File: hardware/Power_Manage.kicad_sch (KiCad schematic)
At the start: 59 parts, among them U10 TPS62088, U4 TPS62088, U6 MAX38904C, U7 MAX38904C, U8 TPS62088, U9 TPS62088

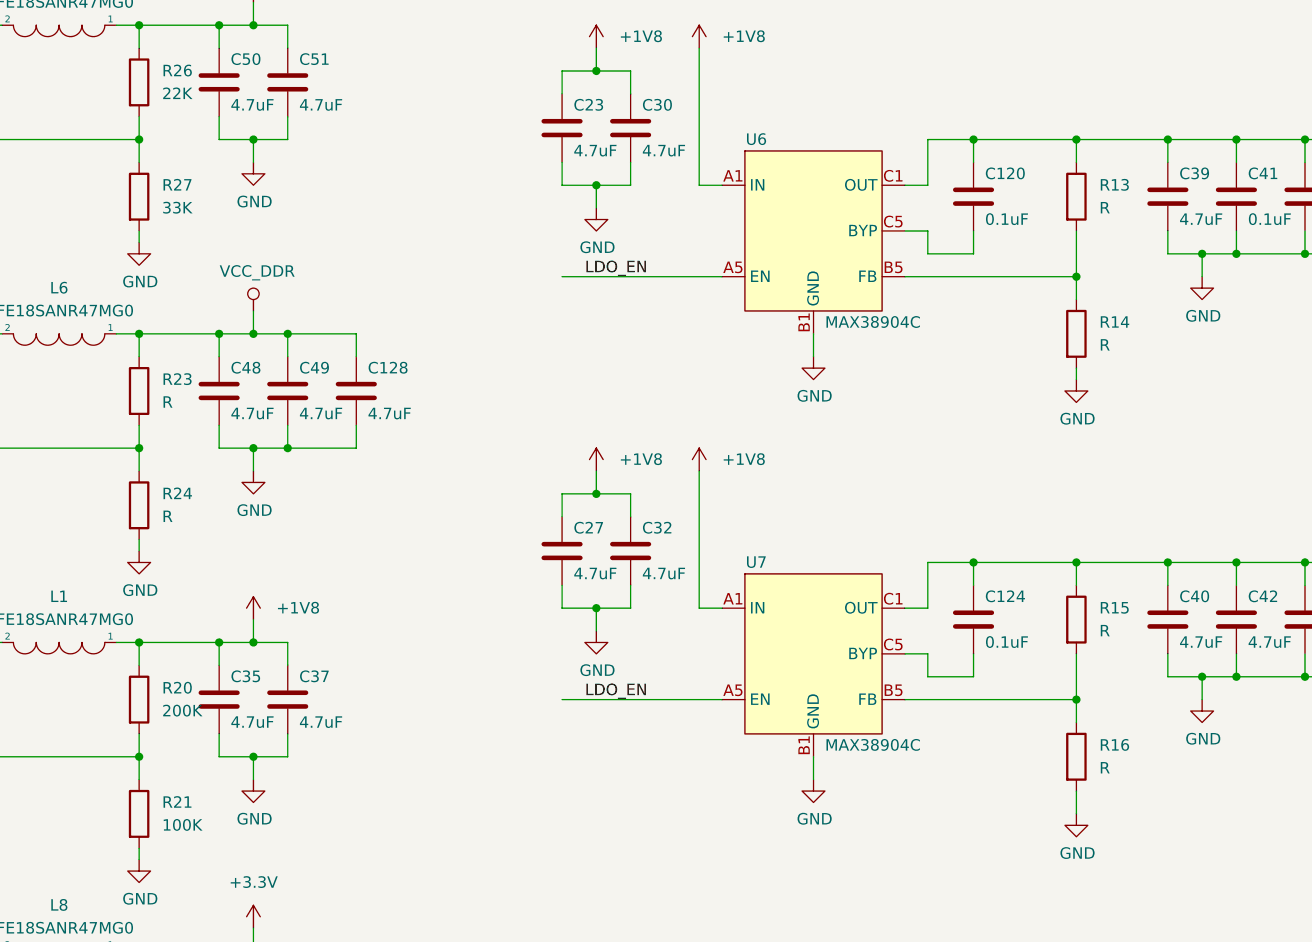
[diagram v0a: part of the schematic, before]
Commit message: add sdio level shift ciruit
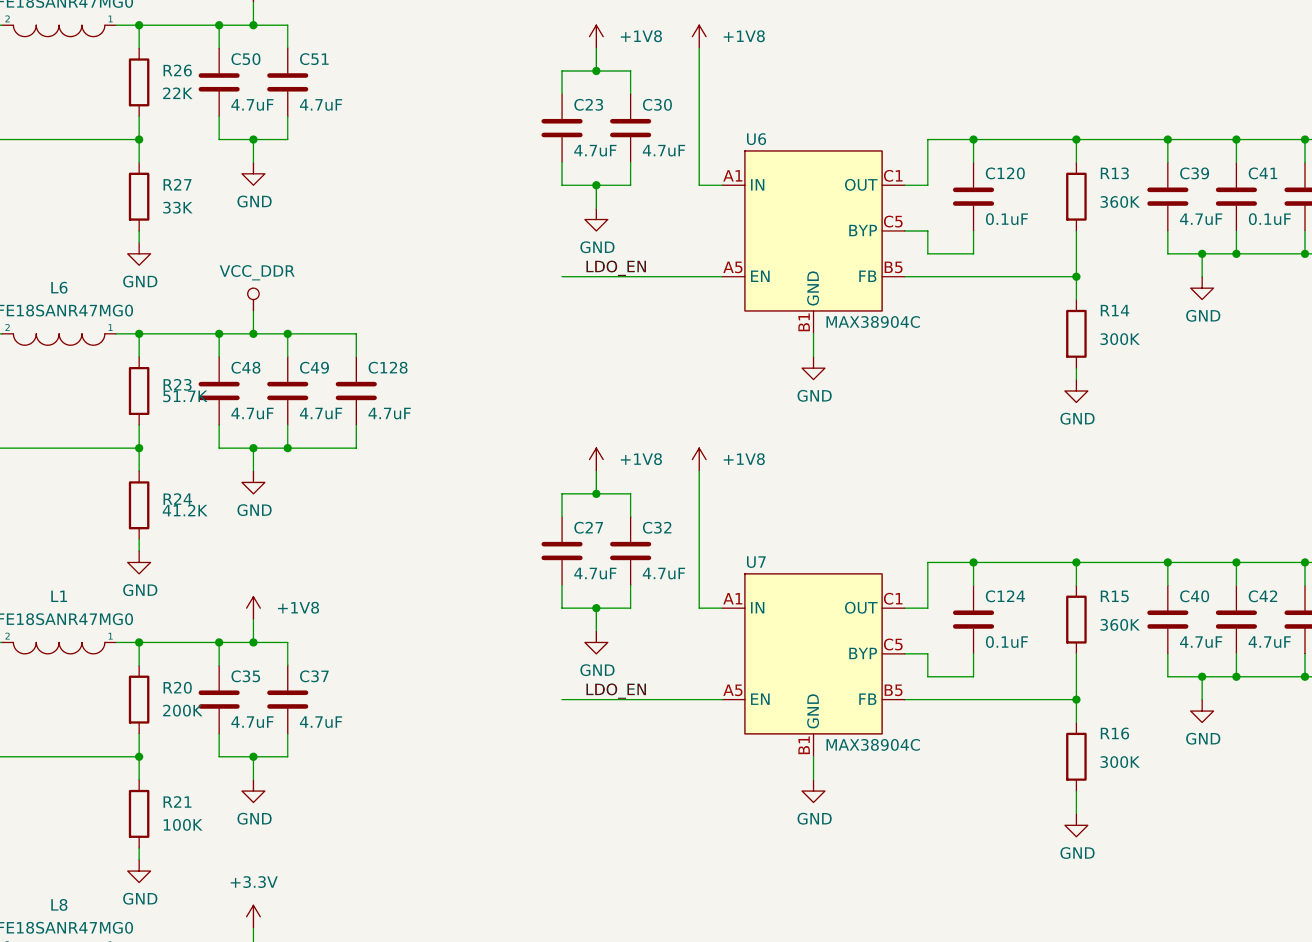
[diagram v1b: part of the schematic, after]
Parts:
- R13, R15: value R -> 360K
- R14, R16: value R -> 300K
- R23: value R -> 51.7K
- R24: value R -> 41.2K
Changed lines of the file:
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@@
-(kicad_sch (version 20220104) (generator eeschema)
+(kicad_sch (version 20220126) (generator eeschema)
   (paper "A3")
   (junction (at 321.31 96.52) (diameter 0) (color 0 0 0 0)
@@
   )
   (symbol (lib_id "Device:R") (at 288.29 90.17 0) (unit 1)
-    (in_bom yes) (on_board yes) (fields_autoplaced)
-    (property "Reference" "R13" (id 0) (at 290.83 88.8999 0)
-      (effects (font (size 1.27 1.27)) (justify left))
-    )
-    (property "Value" "R" (id 1) (at 290.83 91.4399 0)
+    (in_bom yes) (on_board yes)
+    (property "Reference" "R13" (id 0) (at 290.83 87.63 0)
+      (effects (font (size 1.27 1.27)) (justify left))
+    )
+    (property "Value" "360K" (id 1) (at 290.83 90.805 0)
       (effects (font (size 1.27 1.27)) (justify left))
     )
@@
   )
   (symbol (lib_id "Device:R") (at 288.29 152.4 0) (unit 1)
-    (in_bom yes) (on_board yes) (fields_autoplaced)
-    (property "Reference" "R16" (id 0) (at 290.83 151.1299 0)
-      (effects (font (size 1.27 1.27)) (justify left))
-    )
-    (property "Value" "R" (id 1) (at 290.83 153.6699 0)
+    (in_bom yes) (on_board yes)
+    (property "Reference" "R16" (id 0) (at 290.83 149.86 0)
+      (effects (font (size 1.27 1.27)) (justify left))
+    )
+    (property "Value" "300K" (id 1) (at 290.83 153.035 0)
       (effects (font (size 1.27 1.27)) (justify left))
     )
@@
   )
   (symbol (lib_id "Device:R") (at 288.29 105.41 0) (unit 1)
-    (in_bom yes) (on_board yes) (fields_autoplaced)
-    (property "Reference" "R14" (id 0) (at 290.83 104.1399 0)
-      (effects (font (size 1.27 1.27)) (justify left))
-    )
-    (property "Value" "R" (id 1) (at 290.83 106.6799 0)
+    (in_bom yes) (on_board yes)
+    (property "Reference" "R14" (id 0) (at 290.83 102.87 0)
+      (effects (font (size 1.27 1.27)) (justify left))
+    )
+    (property "Value" "300K" (id 1) (at 290.83 106.045 0)
       (effects (font (size 1.27 1.27)) (justify left))
     )
@@
   (symbol (lib_id "Device:R") (at 184.15 111.76 0) (unit 1)
     (in_bom yes) (on_board yes) (fields_autoplaced)
-    (property "Reference" "R23" (id 0) (at 186.69 110.4899 0)
-      (effects (font (size 1.27 1.27)) (justify left))
-    )
-    (property "Value" "R" (id 1) (at 186.69 113.0299 0)
+    (property "Reference" "R23" (id 0) (at 186.69 111.125 0)
+      (effects (font (size 1.27 1.27)) (justify left))
+    )
+    (property "Value" "51.7K" (id 1) (at 186.69 112.395 0)
       (effects (font (size 1.27 1.27)) (justify left))
     )
@@
   )
   (symbol (lib_id "Device:R") (at 288.29 137.16 0) (unit 1)
-    (in_bom yes) (on_board yes) (fields_autoplaced)
-    (property "Reference" "R15" (id 0) (at 290.83 135.8899 0)
-      (effects (font (size 1.27 1.27)) (justify left))
-    )
-    (property "Value" "R" (id 1) (at 290.83 138.4299 0)
+    (in_bom yes) (on_board yes)
+    (property "Reference" "R15" (id 0) (at 290.83 134.62 0)
+      (effects (font (size 1.27 1.27)) (justify left))
+    )
+    (property "Value" "360K" (id 1) (at 290.83 137.795 0)
       (effects (font (size 1.27 1.27)) (justify left))
     )
@@
   (symbol (lib_id "Device:R") (at 184.15 124.46 0) (unit 1)
     (in_bom yes) (on_board yes) (fields_autoplaced)
-    (property "Reference" "R24" (id 0) (at 186.69 123.1899 0)
-      (effects (font (size 1.27 1.27)) (justify left))
-    )
-    (property "Value" "R" (id 1) (at 186.69 125.7299 0)
-      (effects (font (size 1.27 1.27)) (justify left))
-    )
+    (property "Reference" "R24" (id 0) (at 186.69 123.825 0)
+      (effects (font (size 1.27 1.27)) (justify left))
+    )
+    (property "Value" "41.2K" (id 1) (at 186.69 125.095 0)
+      (effects (font (size 1.27 1.27)) (justify left))
+    )

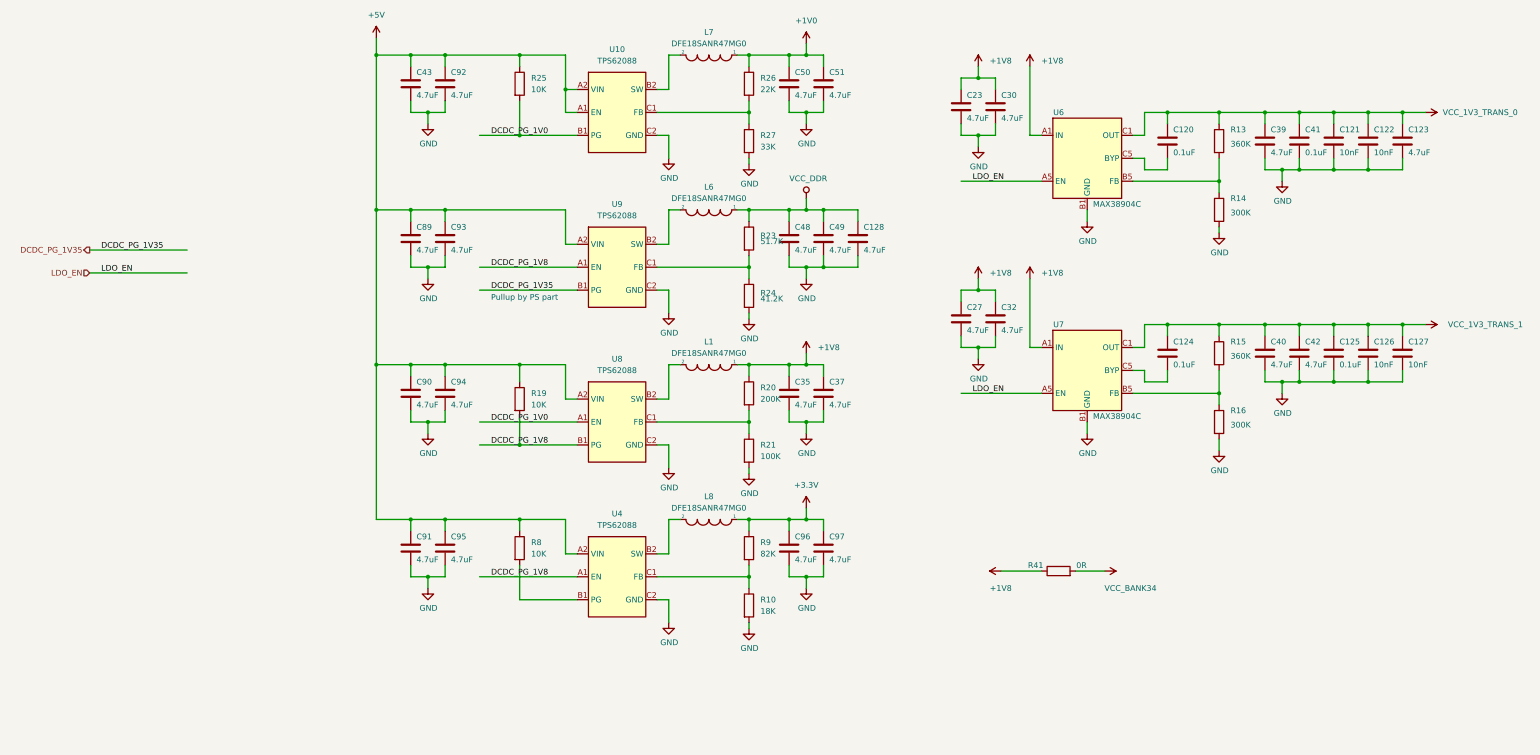
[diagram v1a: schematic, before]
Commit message: Modify wrong DCDC TPS62088 package Panelize PCB Add manufacture requirements files
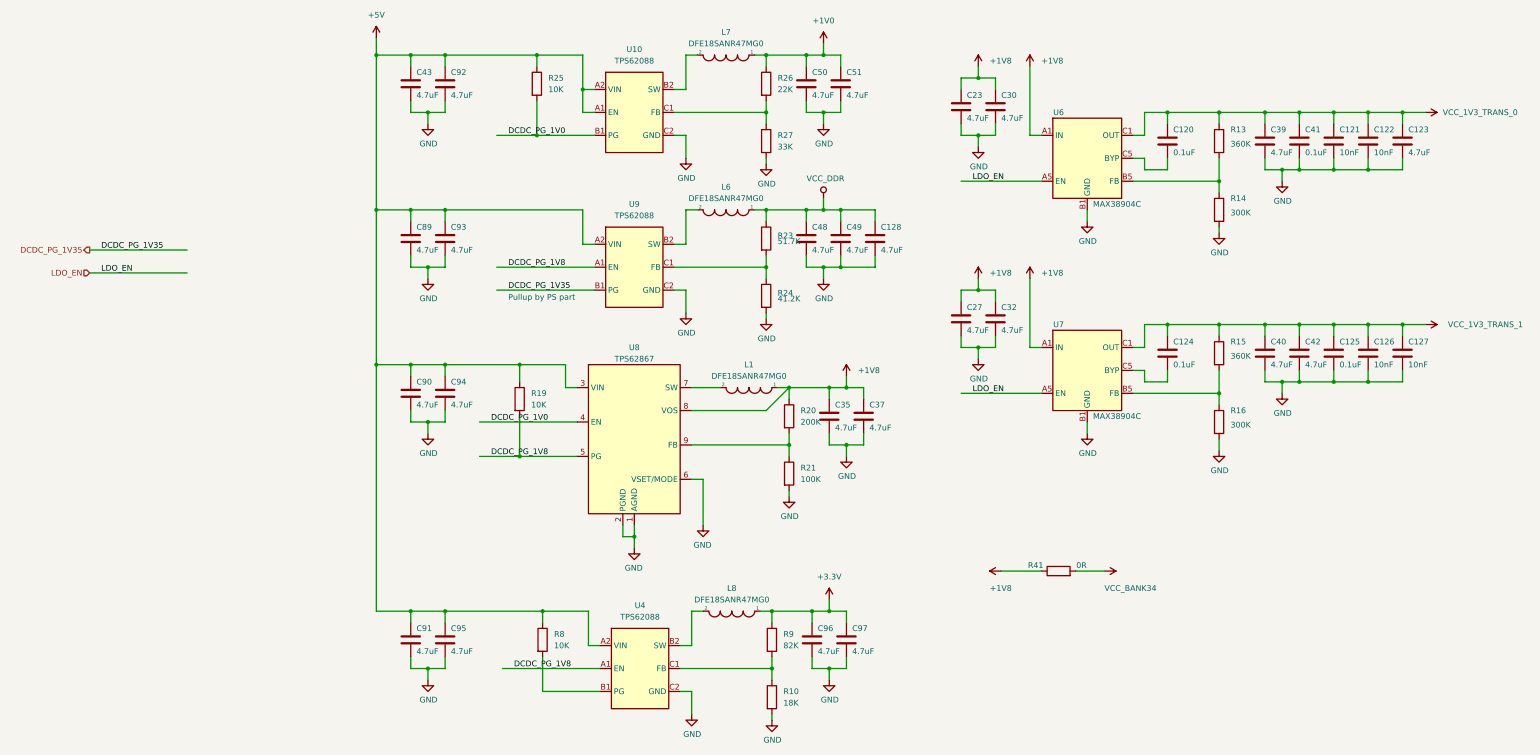
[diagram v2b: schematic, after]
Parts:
- removed U8: TPS62088, Package_CSP:WLCSP-6_1.4x1.0mm_P0.4mm, symbol Power_Supervisor_Local:TPS62088
- added U8: TPS62867, Capacitor_SMD_Local:VQFN-HR, symbol Power_Supervisor_Local:TPS62867
- U10, U4, U9: footprint Package_CSP:WLCSP-6_1.4x1.0mm_P0.4mm -> Capacitor_SMD_Local:PowerWCSP-6
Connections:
- net +1V8: now also U8.8 (VOS)
- net +5V: now also U8.3 (VIN)
- net DCDC_PG_1V0: now also U8.4 (EN)
- net DCDC_PG_1V8: now also U8.5 (PG)
- net GND: now also U8.1 (AGND), U8.2 (PGND), U8.6 (VSET/MODE)
- net at R20.2, R21.1: now also U8.9 (FB)
- net at L1.2: now also U8.7 (SW)
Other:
- moved on the sheet: C128, C35, C37, C48, C49, C50, C51, C91, C95, C96, C97, L1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
